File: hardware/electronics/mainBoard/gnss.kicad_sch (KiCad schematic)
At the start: 28 parts, among them J3 Bus_M.2_Socket_E, J4 M.2 Standoff, J5 M.2 Standoff, SW3 JS102011JCQN, SW4 JS102011JCQN, U7 TPS22996H-Q1, U8 TXS0104VxRUTR, U9 TXS0104VxRUTR

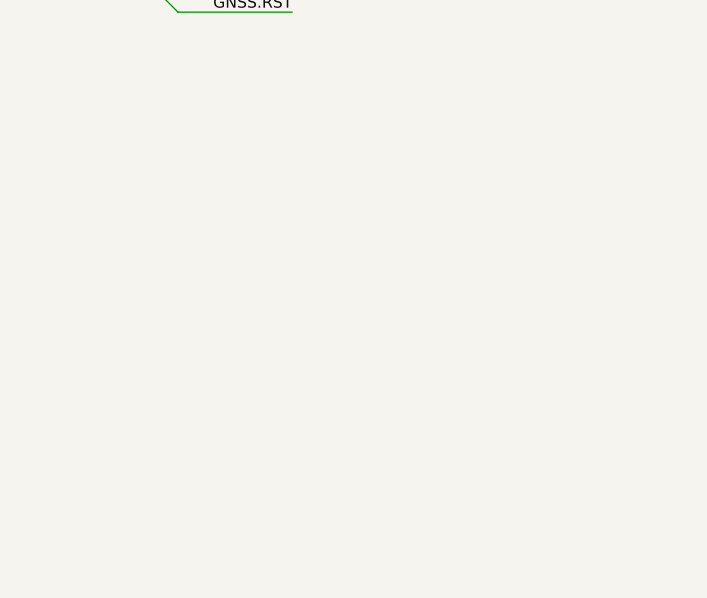
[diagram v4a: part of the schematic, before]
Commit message: added testpoints
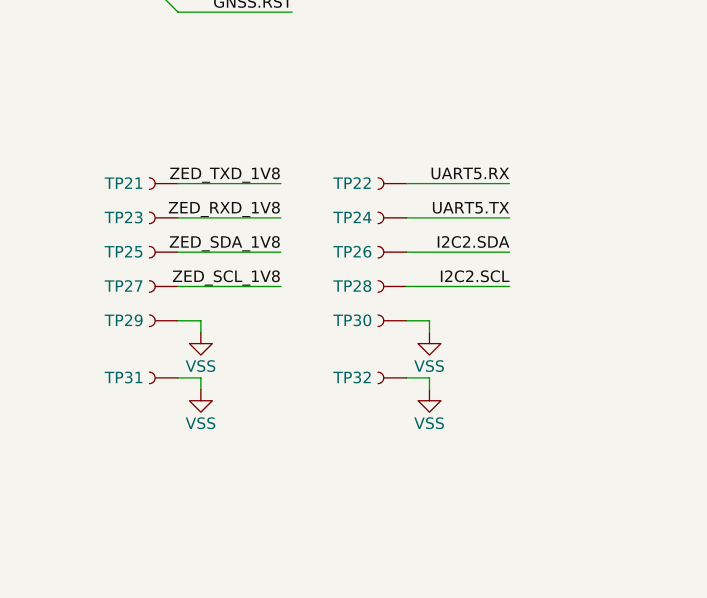
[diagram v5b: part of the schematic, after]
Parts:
- added TP21, TP22, TP23, TP24, TP25, TP26, TP27, TP28: ~, symbol lib_sch:Testpoint
- added TP29, TP30, TP31, TP32: RCWCTE, symbol lib_sch:Testpoint
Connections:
- net I2C2.SCL: now also TP28.1
- net I2C2.SDA: now also TP26.1
- net UART5.RX: now also TP22.1
- net UART5.TX: now also TP24.1
- net VSS: now also TP29.1, TP30.1, TP31.1, TP32.1
- net ZED_RXD_1V8: now also TP23.1
- net ZED_SCL_1V8: now also TP27.1
- net ZED_SDA_1V8: now also TP25.1
- net ZED_TXD_1V8: now also TP21.1

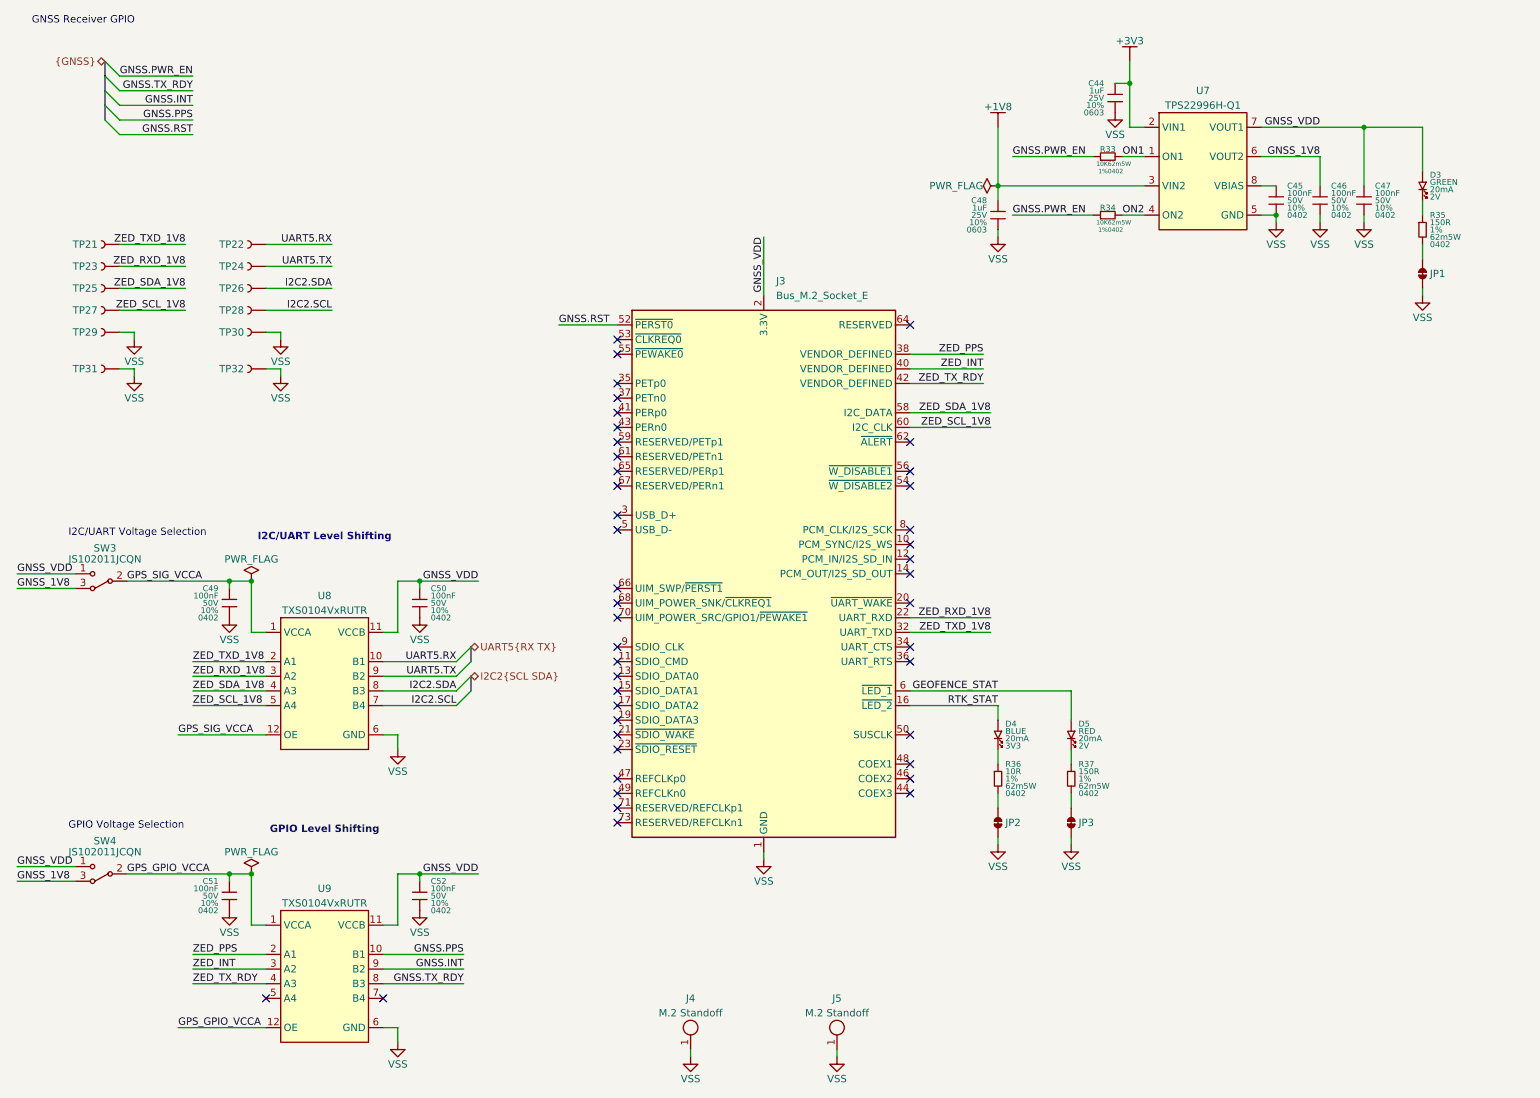
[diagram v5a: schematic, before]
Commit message: updated symbol refs
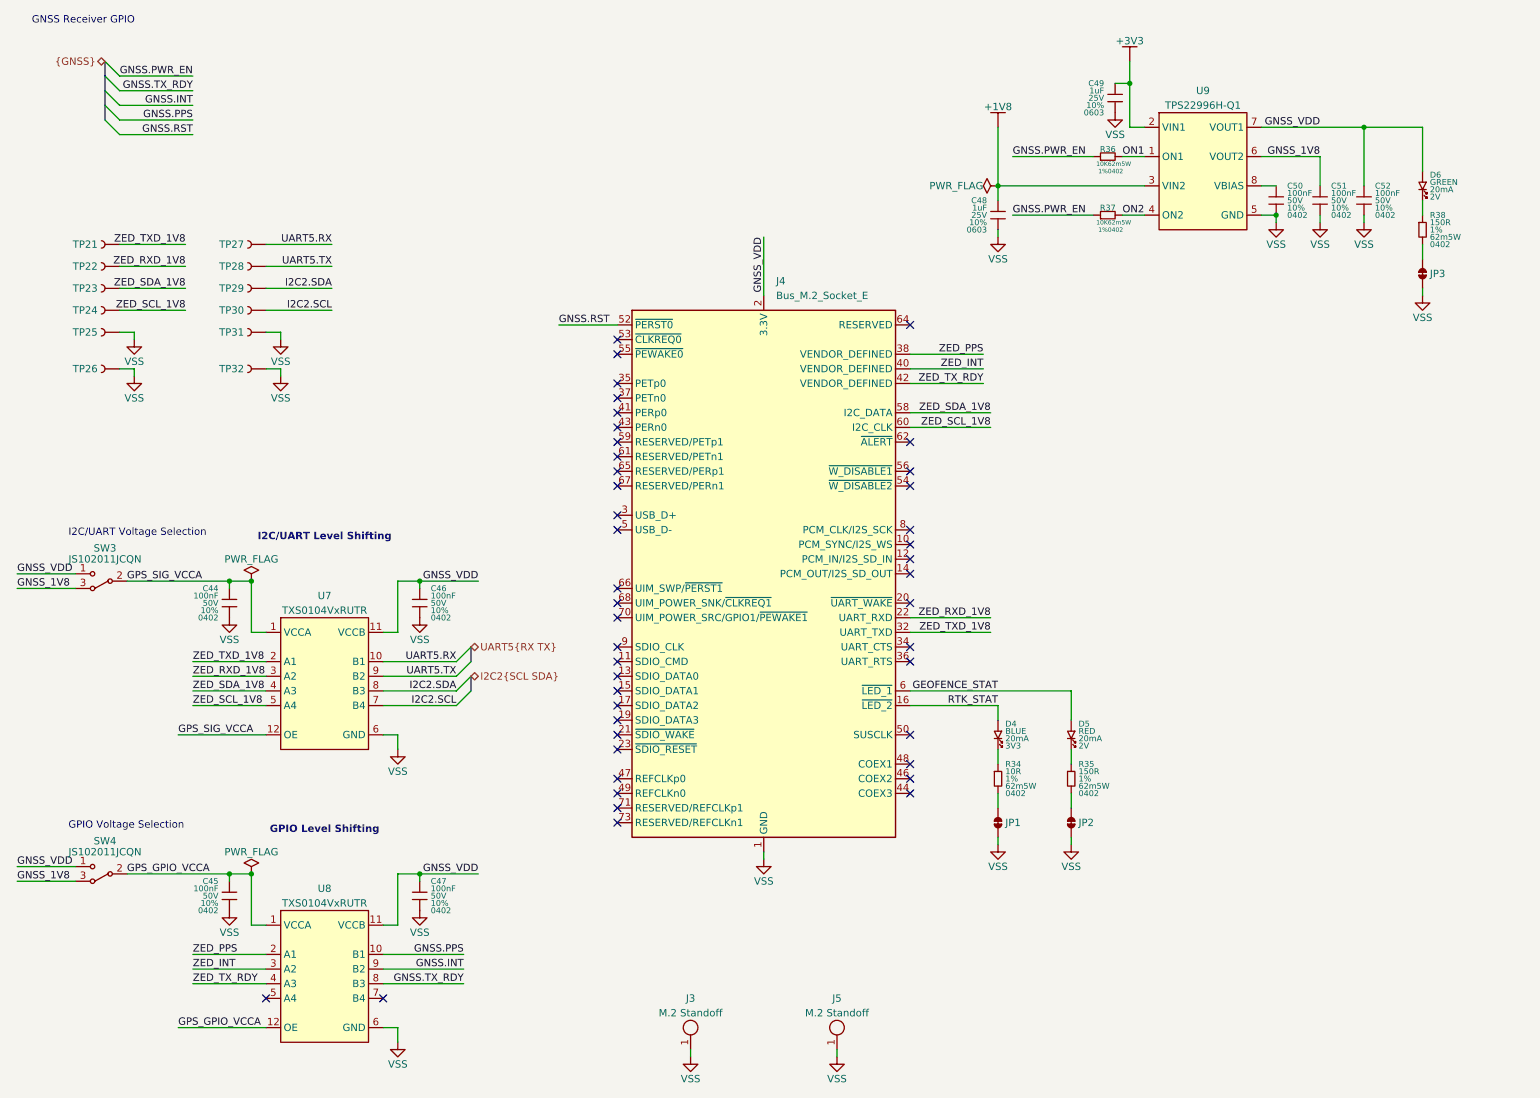
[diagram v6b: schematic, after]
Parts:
- renumbered C49 to C44, C51 to C45, C50 to C46, C52 to C47, C44 to C49, C45 to C50, C46 to C51, C47 to C52, D3 to D6, J4 to J3, J3 to J4, JP2 to JP1, JP3 to JP2, JP1 to JP3, R36 to R34, R37 to R35, R33 to R36, R34 to R37, R35 to R38, TP23 to TP22, TP25 to TP23, TP27 to TP24, TP29 to TP25, TP31 to TP26, TP22 to TP27, TP24 to TP28, TP26 to TP29, TP28 to TP30, TP30 to TP31, U8 to U7, U9 to U8, U7 to U9

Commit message: updated symbol refs
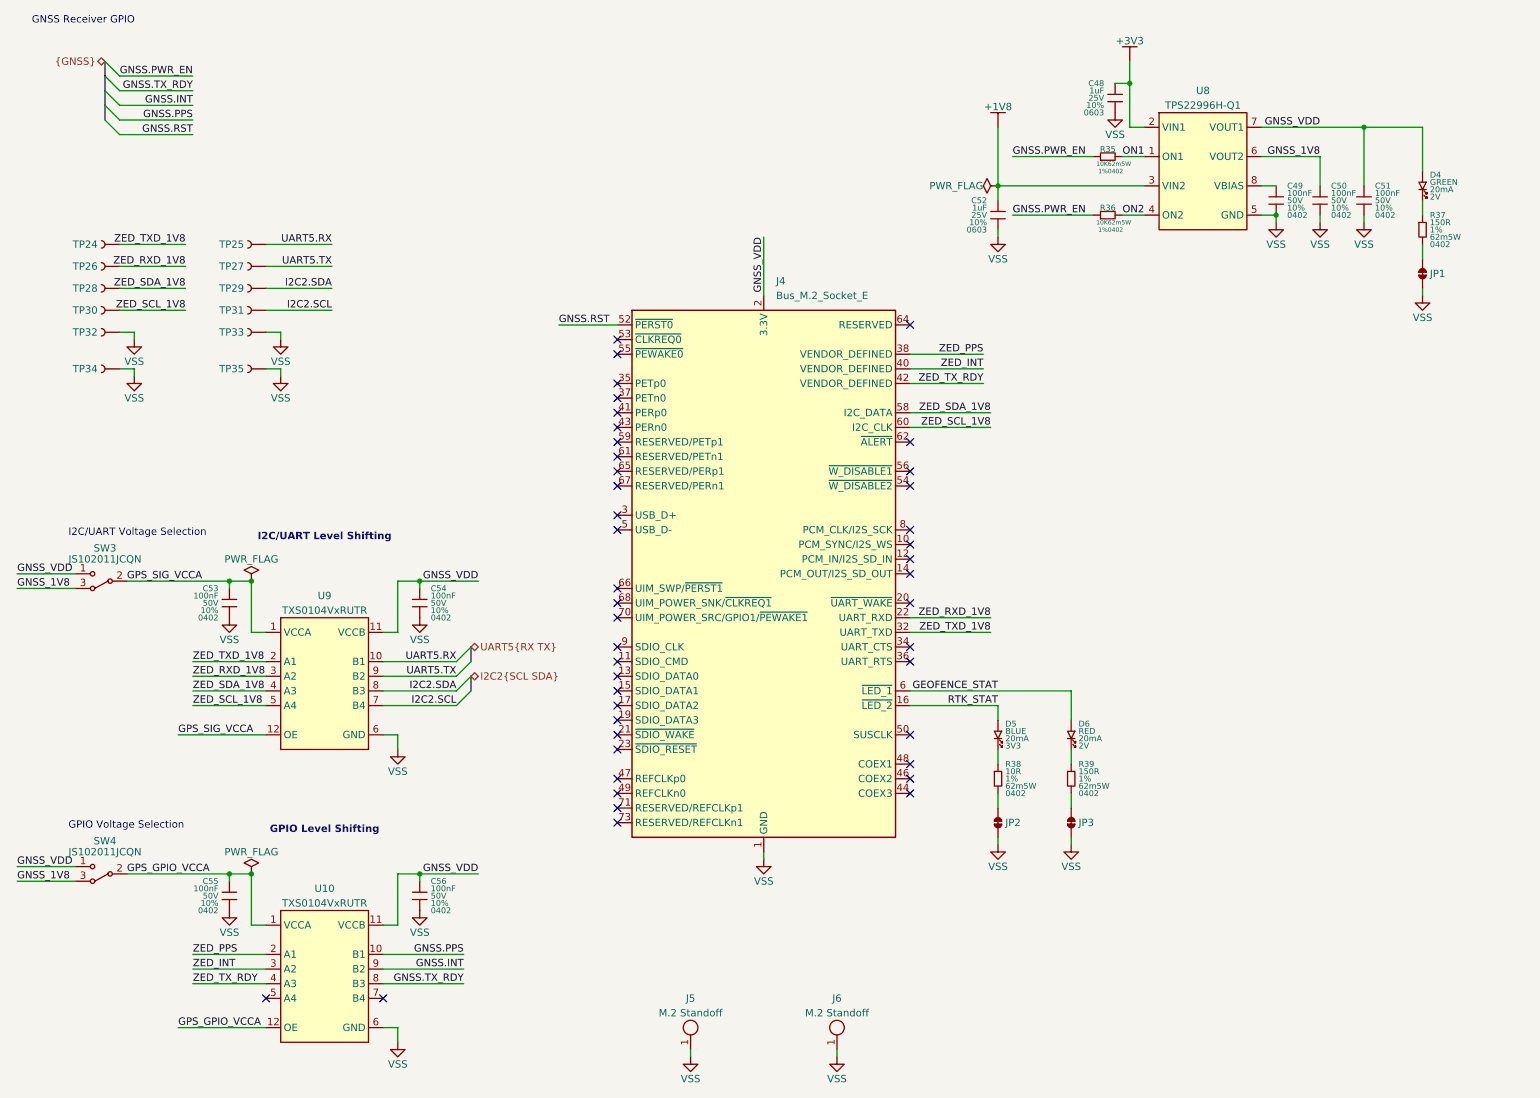
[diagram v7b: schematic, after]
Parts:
- renumbered C49 to C48, C50 to C49, C51 to C50, C52 to C51, C48 to C52, C44 to C53, C46 to C54, C45 to C55, C47 to C56, D6 to D4, D4 to D5, D5 to D6, J3 to J5, J5 to J6, JP3 to JP1, JP1 to JP2, JP2 to JP3, R36 to R35, R37 to R36, R38 to R37, R34 to R38, R35 to R39, TP21 to TP24, TP27 to TP25, TP22 to TP26, TP28 to TP27, TP23 to TP28, TP24 to TP30, TP30 to TP31, TP25 to TP32, TP31 to TP33, TP26 to TP34, TP32 to TP35, U8 to U10, U9 to U8, U7 to U9

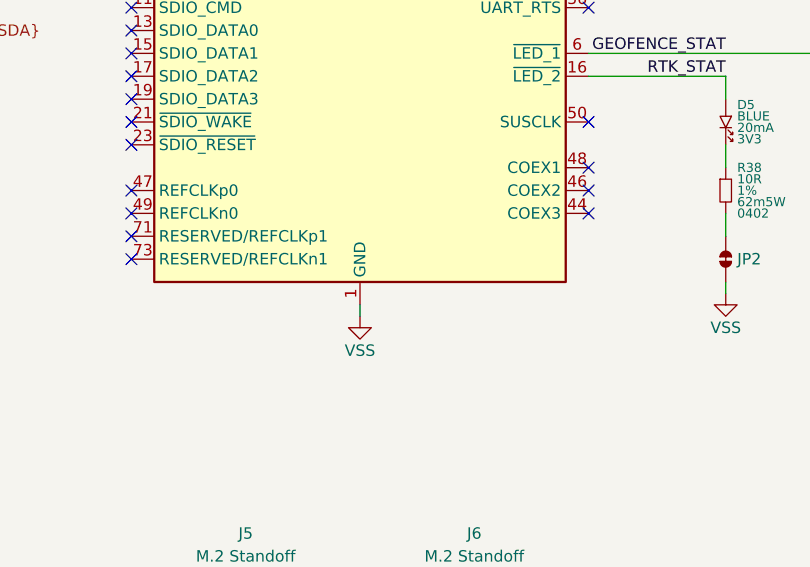
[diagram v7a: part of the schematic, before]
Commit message: assigned FPs
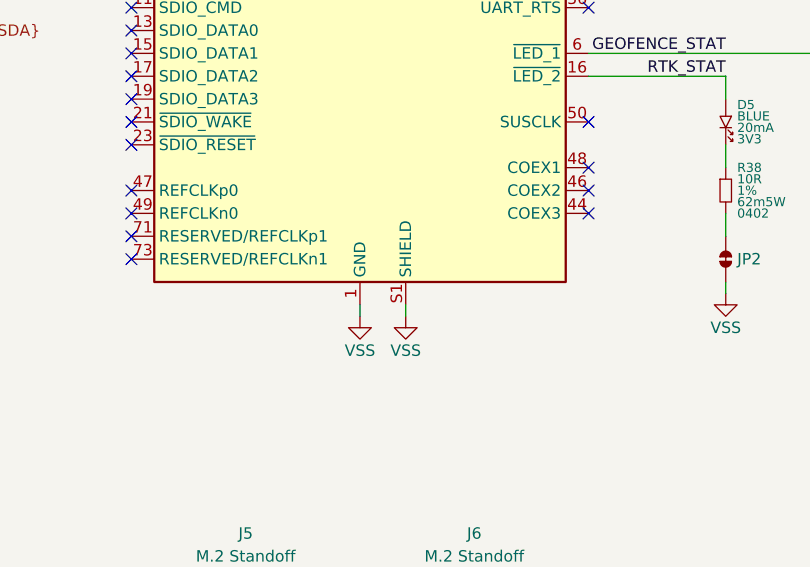
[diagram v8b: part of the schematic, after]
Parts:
- J4: footprint (none) -> lib_connectors:MDT420E01001
- SW3, SW4: footprint (none) -> lib_switches:JS102011JCQN
- U10, U9: footprint (none) -> lib_ICs:QFN40P170X200X55-12
- U8: footprint (none) -> lib_ICs:SOT583
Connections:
- net VSS: now also J4.S1 (SHIELD), J4.S2 (SHIELD)
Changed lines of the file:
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@@
 	(wire
 		(pts
+			(xy 144.78 156.21) (xy 144.78 157.48)
+		)
+		(stroke
+			(width 0)
+			(type default)
+		)
+	)
+	(wire
+		(pts
 			(xy 40.64 128.27) (xy 53.34 128.27)
 		)
@@
 			)
 		)
-		(property "Footprint" ""
+		(property "Footprint" "lib_ICs:SOT583"
 			(at 215.9 38.1 0)
 			(effects
@@
 			)
 		)
-		(property "Footprint" ""
+		(property "Footprint" "lib_switches:JS102011JCQN"
 			(at 25.4 109.22 0)
 			(effects
@@
 			)
 		)
-		(property "Footprint" ""
+		(property "Footprint" "lib_connectors:MDT420E01001"
 			(at 139.7 81.28 0)
 			(effects
@@
 		(pin "53"
 		)
+		(pin "S1"
+		)
+		(pin "S2"
+		)
 		(instances
 			(project ""
@@
 			)
 		)
-		(property "Footprint" ""
+		(property "Footprint" "lib_ICs:QFN40P170X200X55-12"
 			(at 63.5 181.61 0)
 			(effects
@@
 	)
 	(symbol
+		(lib_id "lib_pwr:VSS")
+		(at 144.78 157.48 0)
+		(unit 1)
+		(exclude_from_sim no)
+		(in_bom yes)
+		(on_board yes)
+		(dnp no)
+		(fields_autoplaced yes)
+		(property "Reference" "#PWR0303"
+			(at 144.78 157.48 0)
+			(effects
+				(font
+					(size 1.27 1.27)
+				)
+				(hide yes)
+			)
+		)
+		(property "Value" "VSS"
+			(at 144.78 161.29 0)
+			(do_not_autoplace yes)
+			(effects
+				(font
+					(size 1.27 1.27)
+				)
+			)
+		)
+		(property "Footprint" ""
+			(at 144.78 157.48 0)
+			(effects
+				(font
+					(size 1.27 1.27)
+				)
+				(hide yes)
+			)
+		)
+		(property "Datasheet" ""
+			(at 144.78 157.48 0)
+			(effects
+				(font
+					(size 1.27 1.27)
+				)
+				(hide yes)
+			)
+		)
+		(property "Description" ""
+			(at 144.78 157.48 0)
+			(effects
+				(font
+					(size 1.27 1.27)
+				)
+				(hide yes)
+			)
+		)
+		(pin "1"
+		)
+		(instances
+			(project "mainBoard"
+				(path "/be16e32f-2ccf-4272-9ec7-94d5fe7a55e0/a790e55f-aead-4e0e-93f9-b61f88112fc6"
+					(reference "#PWR0303")
+					(unit 1)
+				)
+			)
+		)
+	)
+	(symbol
 		(lib_id "lib_sch:R")
 		(at 193.04 143.51 0)
@@
 			)
 		)
-		(property "Footprint" ""
+		(property "Footprint" "lib_ICs:QFN40P170X200X55-12"
 			(at 63.5 130.81 0)
 			(effects
@@
 			)
 		)
-		(property "Footprint" ""
+		(property "Footprint" "lib_switches:JS102011JCQN"
 			(at 25.4 160.02 0)
 			(effects
